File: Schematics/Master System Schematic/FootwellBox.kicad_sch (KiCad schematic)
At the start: 9 parts, among them U4 KY-019, U5 CAN_Bus_Module, U6 CAN_Bus_Module

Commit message: Updated master sheet title
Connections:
- new net: A1.~ (~D9), U6.~ (Serial_Clock) (x5)
- new net: A2.~ (~D9), U5.~ (Serial_Clock) (x5)

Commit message: Added missing 12V in latching
Missing 12V to CAN fault pole
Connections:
- new net: A1.~ (~D9), U6.~ (Serial_Clock) (x5)
- new net: A2.~ (~D9), U5.~ (Serial_Clock) (x5)

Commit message: Added charge connector and charge detection
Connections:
- new net: A1.~ (~D9), U6.~ (Serial_Clock) (x5)
- new net: A2.~ (~D9), U5.~ (Serial_Clock) (x5)

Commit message: Moved Side BRB
Returned to pre fuse box location
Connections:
- new net: A1.~ (~D9), U6.~ (Serial_Clock) (x5)
- new net: A2.~ (~D9), U5.~ (Serial_Clock) (x5)

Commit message: Update for color coding
Update for color coding
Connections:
- new net: A1.~ (~D9), U6.~ (Serial_Clock) (x5)
- new net: A2.~ (~D9), U5.~ (Serial_Clock) (x5)

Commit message: update color and add fan
update color and add fan
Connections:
- new net: A1.~ (~D9), U6.~ (Serial_Clock) (x5)
- new net: A2.~ (~D9), U5.~ (Serial_Clock) (x5)
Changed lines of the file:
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@@
+    (effects (font (size 1.27 1.27)) (justify right))
+  )
+  (hierarchical_label "Radiator_Fan_Control" (shape input) (at 56.515 224.155 180)
     (effects (font (size 1.27 1.27)) (justify right))
   )

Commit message: further update
further update
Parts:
- added M?: MNMOS, symbol pspice:MNMOS
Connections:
- net GND: now also M?.3 (S), M?.4 (B)
- net Radiator_Fan_Control: now also M?.1 (D)
- new net: A1.~ (~D9), U6.~ (Serial_Clock) (x5)
- new net: A2.~ (~D9), U5.~ (Serial_Clock) (x5)
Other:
- note added: "18AWG"
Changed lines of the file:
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@@
   (junction (at 90.17 251.46) (diameter 0) (color 0 0 0 0)
   )
+  (junction (at 71.12 251.46) (diameter 0) (color 0 0 0 0)
+  )
   (junction (at 299.72 267.97) (diameter 0) (color 0 0 0 0)
   )
@@
   )
   (junction (at 185.42 288.29) (diameter 0) (color 0 0 0 0)
+  )
+  (junction (at 68.58 251.46) (diameter 0) (color 0 0 0 0)
   )
   (no_connect (at 157.48 160.02))
@@
     (stroke (width 0) (type default) (color 0 0 0 0))
   )
+  (wire (pts (xy 220.98 152.4) (xy 257.81 152.4))
+    (stroke (width 0) (type default) (color 0 0 0 0))
+  )
   (wire (pts (xy 299.72 267.97) (xy 299.72 148.59))
     (stroke (width 0) (type default) (color 0 0 0 0))
@@
     (stroke (width 0) (type default) (color 0 0 0 0))
   )
+  (wire (pts (xy 71.12 251.46) (xy 90.17 251.46))
+    (stroke (width 0) (type default) (color 0 0 0 0))
+  )
   (wire (pts (xy 149.86 224.79) (xy 130.81 224.79))
     (stroke (width 0) (type default) (color 0 0 0 0))
@@
     (stroke (width 0) (type default) (color 0 0 0 0))
   )
-  (wire (pts (xy 214.63 151.13) (xy 214.63 149.86))
-    (stroke (width 0) (type default) (color 0 0 0 0))
-  )
   (wire (pts (xy 135.89 280.67) (xy 135.89 287.02))
     (stroke (width 0) (type default) (color 0 0 0 0))
   )
-  (wire (pts (xy 214.63 151.13) (xy 228.6 151.13))
-    (stroke (width 0) (type default) (color 0 0 0 0))
-  )
   (wire (pts (xy 116.84 326.39) (xy 116.84 251.46))
     (stroke (width 0) (type default) (color 0 0 0 0))
@@
     (stroke (width 0) (type default) (color 0 0 0 0))
   )
-  (wire (pts (xy 187.96 149.86) (xy 214.63 149.86))
+  (wire (pts (xy 71.12 241.935) (xy 71.12 251.46))
     (stroke (width 0) (type default) (color 0 0 0 0))
   )
@@
     (stroke (width 0) (type default) (color 0 0 0 0))
   )
+  (wire (pts (xy 68.58 251.46) (xy 71.12 251.46))
+    (stroke (width 0) (type default) (color 0 0 0 0))
+  )
+  (wire (pts (xy 71.12 224.155) (xy 56.515 224.155))
+    (stroke (width 0) (type default) (color 194 194 0 1))
+  )
   (wire (pts (xy 185.42 288.29) (xy 193.04 288.29))
     (stroke (width 0) (type default) (color 0 0 0 0))
@@
     (stroke (width 0) (type default) (color 0 0 0 0))
   )
+  (wire (pts (xy 187.96 149.86) (xy 218.44 149.86))
+    (stroke (width 0) (type default) (color 0 0 0 0))
+  )
   (wire (pts (xy 173.99 293.37) (xy 186.69 293.37))
     (stroke (width 0) (type default) (color 0 0 0 0))
@@
     (stroke (width 0) (type default) (color 0 0 0 0))
   )
+  (wire (pts (xy 68.58 241.935) (xy 68.58 251.46))
+    (stroke (width 0) (type default) (color 0 0 0 0))
+  )
   (wire (pts (xy 214.63 198.12) (xy 214.63 185.42))
     (stroke (width 0) (type default) (color 0 0 0 0))
@@
     (stroke (width 0) (type default) (color 0 0 0 0))
   )
-  (wire (pts (xy 257.81 152.4) (xy 228.6 152.4))
-    (stroke (width 0) (type default) (color 0 0 0 0))
-  )
   (wire (pts (xy 60.96 264.16) (xy 60.96 266.7))
     (stroke (width 0) (type default) (color 0 0 0 0))
@@
     (stroke (width 0) (type default) (color 0 0 0 0))
   )
+  (wire (pts (xy 71.12 231.775) (xy 71.12 224.155))
+    (stroke (width 0) (type default) (color 194 194 0 1))
+  )
   (wire (pts (xy 187.96 173.99) (xy 219.71 173.99))
     (stroke (width 0) (type default) (color 0 0 0 0))
@@
     (stroke (width 0) (type default) (color 0 0 0 0))
   )
-  (wire (pts (xy 194.31 269.24) (xy 194.31 271.78))
-    (stroke (width 0) (type default) (color 0 0 0 0))
-  )
   (wire (pts (xy 128.27 227.33) (xy 149.86 227.33))
     (stroke (width 0) (type default) (color 0 0 0 0))
@@
     (stroke (width 0) (type default) (color 0 0 0 0))
   )
-  (wire (pts (xy 190.5 270.51) (xy 190.5 269.24))
-    (stroke (width 0) (type default) (color 0 0 0 0))
-  )
   (wire (pts (xy 69.215 219.71) (xy 56.515 219.71))
     (stroke (width 0) (type default) (color 0 0 0 0))
   )
-  (wire (pts (xy 228.6 152.4) (xy 228.6 151.13))
-    (stroke (width 0) (type default) (color 0 0 0 0))
-  )
   (wire (pts (xy 147.32 171.45) (xy 130.81 171.45))
     (stroke (width 0) (type default) (color 0 0 0 0))
   )
-  (wire (pts (xy 218.44 149.86) (xy 218.44 152.4))
+  (wire (pts (xy 220.98 149.86) (xy 218.44 152.4))
     (stroke (width 0) (type default) (color 0 0 0 0))
   )
@@
     (stroke (width 0) (type default) (color 0 0 0 0))
   )
-  (wire (pts (xy 198.12 271.78) (xy 264.16 271.78))
-    (stroke (width 0) (type default) (color 0 0 0 0))
-  )
   (wire (pts (xy 198.12 293.37) (xy 198.12 302.26))
     (stroke (width 0) (type default) (color 0 0 0 0))
@@
     (stroke (width 0) (type default) (color 0 0 0 0))
   )
-  (wire (pts (xy 198.12 270.51) (xy 198.12 271.78))
+  (wire (pts (xy 196.85 271.78) (xy 264.16 271.78))
     (stroke (width 0) (type default) (color 0 0 0 0))
   )
@@
     (stroke (width 0) (type default) (color 0 0 0 0))
   )
-  (wire (pts (xy 190.5 270.51) (xy 198.12 270.51))
-    (stroke (width 0) (type default) (color 0 0 0 0))
-  )
   (wire (pts (xy 187.96 147.32) (xy 257.81 147.32))
     (stroke (width 0) (type default) (color 0 0 0 0))
@@
     (stroke (width 0) (type default) (color 0 0 0 0))
   )
+  (wire (pts (xy 194.31 269.24) (xy 196.85 271.78))
+    (stroke (width 0) (type default) (color 0 0 0 0))
+  )
   (wire (pts (xy 299.72 148.59) (xy 287.02 148.59))
     (stroke (width 0) (type default) (color 0 0 0 0))
@@
     (stroke (width 0) (type default) (color 0 0 0 0))
   )
+  (wire (pts (xy 196.85 269.24) (xy 264.16 269.24))
+    (stroke (width 0) (type default) (color 0 0 0 0))
+  )
   (wire (pts (xy 297.18 274.32) (xy 293.37 274.32))
     (stroke (width 0) (type default) (color 0 0 0 0))
@@
     (stroke (width 0) (type default) (color 0 0 0 0))
   )
-  (wire (pts (xy 190.5 269.24) (xy 173.99 269.24))
-    (stroke (width 0) (type default) (color 0 0 0 0))
-  )
   (wire (pts (xy 187.96 154.94) (xy 257.81 154.94))
     (stroke (width 0) (type default) (color 0 0 0 0))
@@
     (stroke (width 0) (type default) (color 0 0 0 0))
   )
+  (wire (pts (xy 173.99 269.24) (xy 194.31 269.24))
+    (stroke (width 0) (type default) (color 0 0 0 0))
+  )
   (wire (pts (xy 177.8 231.14) (xy 177.8 251.46))
     (stroke (width 0) (type default) (color 0 0 0 0))
   )
-  (wire (pts (xy 194.31 269.24) (xy 264.16 269.24))
-    (stroke (width 0) (type default) (color 0 0 0 0))
-  )
   (wire (pts (xy 207.01 264.16) (xy 207.01 276.86))
     (stroke (width 0) (type default) (color 0 0 0 0))
@@
     (stroke (width 0) (type default) (color 0 0 0 0))
   )
+  (wire (pts (xy 218.44 149.86) (xy 220.98 152.4))
+    (stroke (width 0) (type default) (color 0 0 0 0))
+  )
   (wire (pts (xy 214.63 171.45) (xy 219.71 171.45))
     (stroke (width 0) (type default) (color 0 0 0 0))
@@
     (stroke (width 0) (type default) (color 0 0 0 0))
   )
-  (wire (pts (xy 60.96 251.46) (xy 90.17 251.46))
+  (wire (pts (xy 220.98 149.86) (xy 257.81 149.86))
+    (stroke (width 0) (type default) (color 0 0 0 0))
+  )
+  (wire (pts (xy 60.96 251.46) (xy 68.58 251.46))
     (stroke (width 0) (type default) (color 0 0 0 0))
   )
@@
     (stroke (width 0) (type default) (color 0 0 0 0))
   )
+  (wire (pts (xy 196.85 269.24) (xy 194.31 271.78))
+    (stroke (width 0) (type default) (color 0 0 0 0))
+  )
   (wire (pts (xy 135.89 276.86) (xy 143.51 276.86))
     (stroke (width 0) (type default) (color 0 0 0 0))
@@
     (stroke (width 0) (type default) (color 0 0 0 0))
   )
-  (wire (pts (xy 218.44 149.86) (xy 257.81 149.86))
-    (stroke (width 0) (type default) (color 0 0 0 0))
-  )
   (wire (pts (xy 60.96 266.7) (xy 57.15 266.7))
     (stroke (width 0) (type default) (color 0 0 0 0))
@@
   (wire (pts (xy 109.22 287.02) (xy 135.89 287.02))
     (stroke (width 0) (type default) (color 0 0 0 0))
+  )
+  (text "18AWG" (at 58.42 224.155 0)
+    (effects (font (size 1.27 1.27)) (justify left bottom))
   )
   (hierarchical_label "POT1+" (shape input) (at 130.81 166.37 180)
@@
     (pin "2")
   )
+  (symbol (lib_id "pspice:MNMOS") (at 73.66 236.855 0) (mirror y) (unit 1)
+    (in_bom yes) (on_board yes)
+    (property "Reference" "M?" (id 0) (at 66.675 235.585 0)
+      (effects (font (size 1.27 1.27)) (justify left))
+    )
+    (property "Value" "MNMOS" (id 1) (at 66.675 238.125 0)
+      (effects (font (size 1.27 1.27)) (justify left))
+    )
+    (property "Footprint" "" (id 2) (at 74.295 236.855 0)
+      (effects (font (size 1.27 1.27)) hide)
+    )
+    (property "Datasheet" "~" (id 3) (at 74.295 236.855 0)
+      (effects (font (size 1.27 1.27)) hide)
+    )
+    (pin "1")
+    (pin "2")
+    (pin "3")
+    (pin "4")
+  )
   (symbol (lib_id "Device:R") (at 190.5 293.37 90) (unit 1)

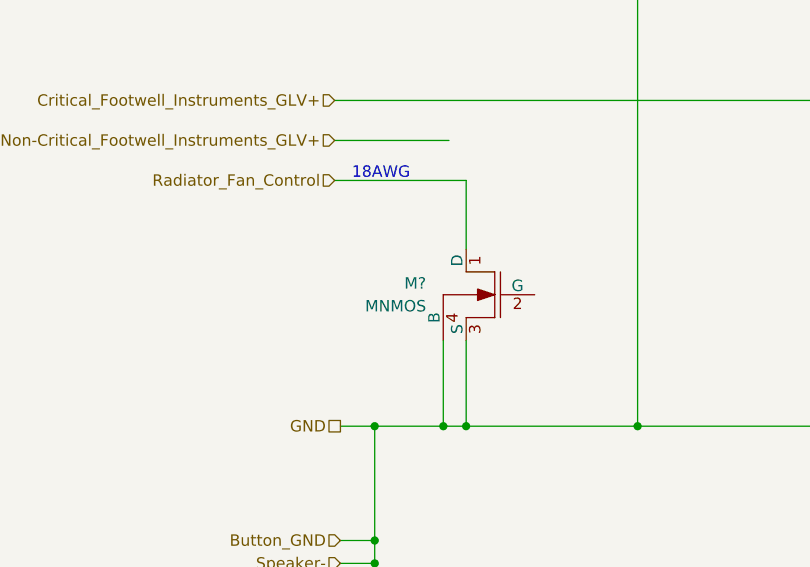
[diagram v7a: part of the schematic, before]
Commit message: Master schematic fixes
- readded charge backpower
- Added Driver io LV batt guage
- Thickened wires
- swapped 2awg to 35mm2
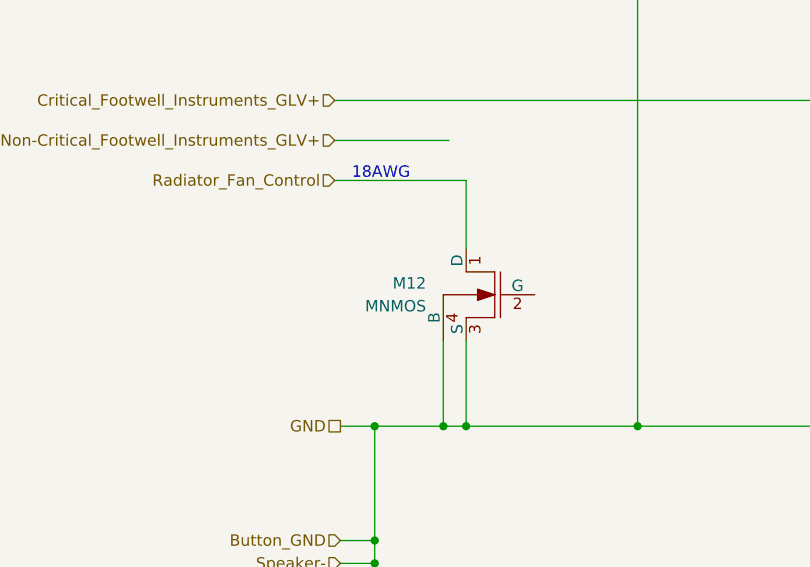
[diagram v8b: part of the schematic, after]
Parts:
- gave numbers to parts that had none: 1
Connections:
- new net: A1.~ (~D9), U6.~ (Serial_Clock) (x5)
- new net: A2.~ (~D9), U5.~ (Serial_Clock) (x5)
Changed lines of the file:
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@@
   (symbol (lib_id "pspice:MNMOS") (at 73.66 236.855 0) (mirror y) (unit 1)
     (in_bom yes) (on_board yes)
-    (property "Reference" "M?" (id 0) (at 66.675 235.585 0)
+    (property "Reference" "M12" (id 0) (at 66.675 235.585 0)
       (effects (font (size 1.27 1.27)) (justify left))
     )
